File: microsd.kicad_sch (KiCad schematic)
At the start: 14 parts, among them J4 Micro_SD_Card

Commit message: Radio (#22)
* MetrocketryRadio

* Fix: moved radio to schematic hierachy

* Cubemx+schematic update

* Screenshots of updates

* Add files via upload

* fix: schematic fix

---------

Co-authored-by: Kisa <kisahassan770@gmail.com>
Co-authored-by: deadman_kisa <74790048+kiki-hassan@users.noreply.github.com>
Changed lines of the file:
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@@
+	(wire
+		(pts
+			(xy 146.05 106.68) (xy 158.75 106.68)
+		)
+		(stroke
+			(width 0)
+			(type default)
+		)
+	)
 	(wire
 		(pts
@@
 	(wire
 		(pts
-			(xy 147.32 106.68) (xy 158.75 106.68)
-		)
-		(stroke
-			(width 0)
-			(type default)
-		)
-	)
-	(wire
-		(pts
 			(xy 129.54 73.66) (xy 135.89 73.66)
 		)
@@
 		(pts
 			(xy 113.03 125.73) (xy 113.03 133.35)
+		)
+		(stroke
+			(width 0)
+			(type default)
+		)
+	)
+	(wire
+		(pts
+			(xy 146.05 116.84) (xy 146.05 106.68)
 		)
 		(stroke
@@
 	(symbol
 		(lib_id "power:GND")
-		(at 147.32 106.68 270)
+		(at 146.05 116.84 0)
 		(unit 1)
 		(body_style 1)
@@
 		(fields_autoplaced yes)
 		(property "Reference" "#PWR042"
-			(at 140.97 106.68 0)
+			(at 146.05 123.19 0)
 			(hide yes)
 			(show_name no)
@@
 		)
 		(property "Value" "GND"
-			(at 143.51 106.6799 90)
+			(at 146.0499 120.65 90)
 			(hide yes)
 			(show_name no)
@@
 		)
 		(property "Footprint" ""
-			(at 147.32 106.68 0)
+			(at 146.05 116.84 0)
 			(hide yes)
 			(show_name no)
@@
 		)
 		(property "Datasheet" ""
-			(at 147.32 106.68 0)
+			(at 146.05 116.84 0)
 			(hide yes)
 			(show_name no)
@@
 		)
 		(property "Description" "Power symbol creates a global label with name \"GND\" , ground"
-			(at 147.32 106.68 0)
+			(at 146.05 116.84 0)
 			(hide yes)
 			(show_name no)
@@
 		)
 	)
+	(embedded_fonts no)
 )

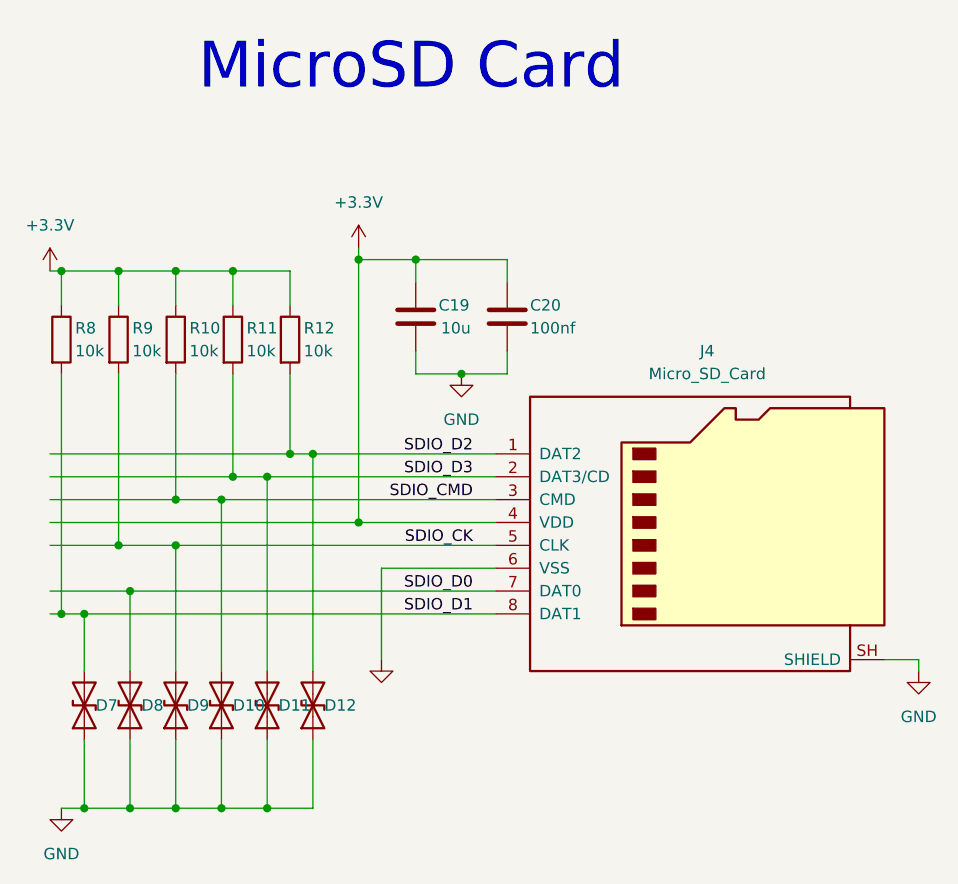
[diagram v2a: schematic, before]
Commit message: Fixed GPS, Radio, Baro, STM32, and added/rearanged some sheets (#26)
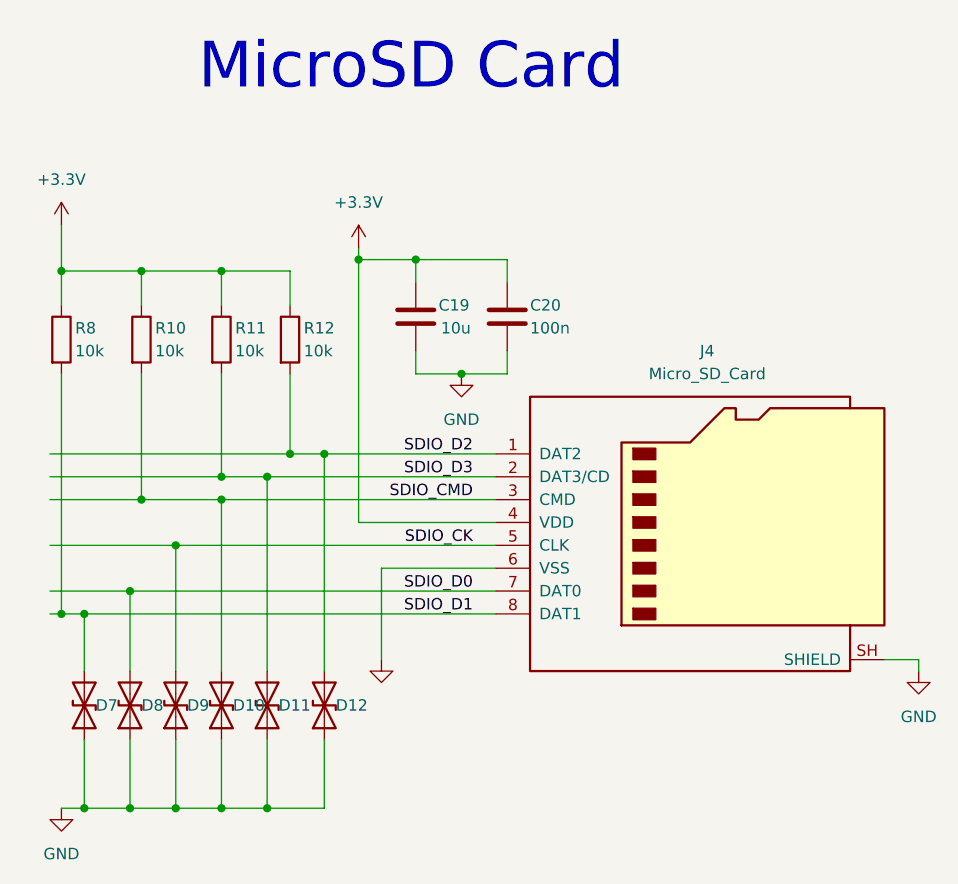
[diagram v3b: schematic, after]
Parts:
- removed R9: 10k, symbol Device:R
- C20: value 100nf -> 100n
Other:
- moved on the sheet: D12, R10, R11
